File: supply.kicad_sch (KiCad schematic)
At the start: 98 parts, among them J12 Molex_Nano-Fit-105430_xx02-ho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, Q11 PJE138K, Q13 BCM857BS-7-F, Q14 BCM857BS-7-F, Q15 SSM3J332R, Q16 SSM3J332R, Q18 SSM3J332R, Q5 PJE138K, Q6 SSM3J332R, Q7 PJE138K, Q8 PJE138K, SW1 PCM12SMTR, U1 TPS56C230, U29 TPS56C230, U37 74LVC2G14GV, U38 74LVC1G175GV, U41 NCP730BMT330TBG, U42 TPS7A0518PDBVT

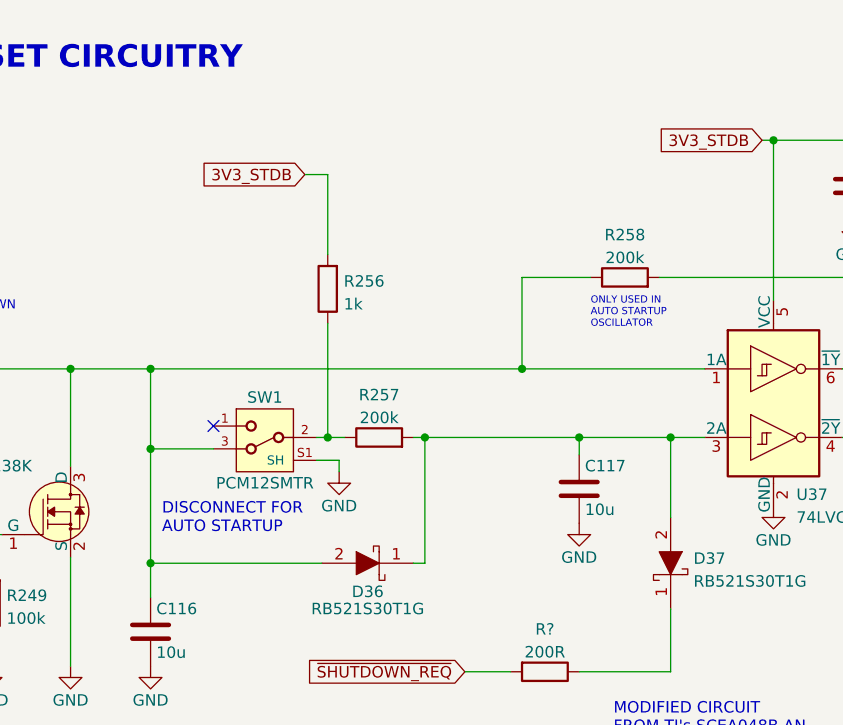
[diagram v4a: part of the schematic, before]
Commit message: Clarify auto startup comments
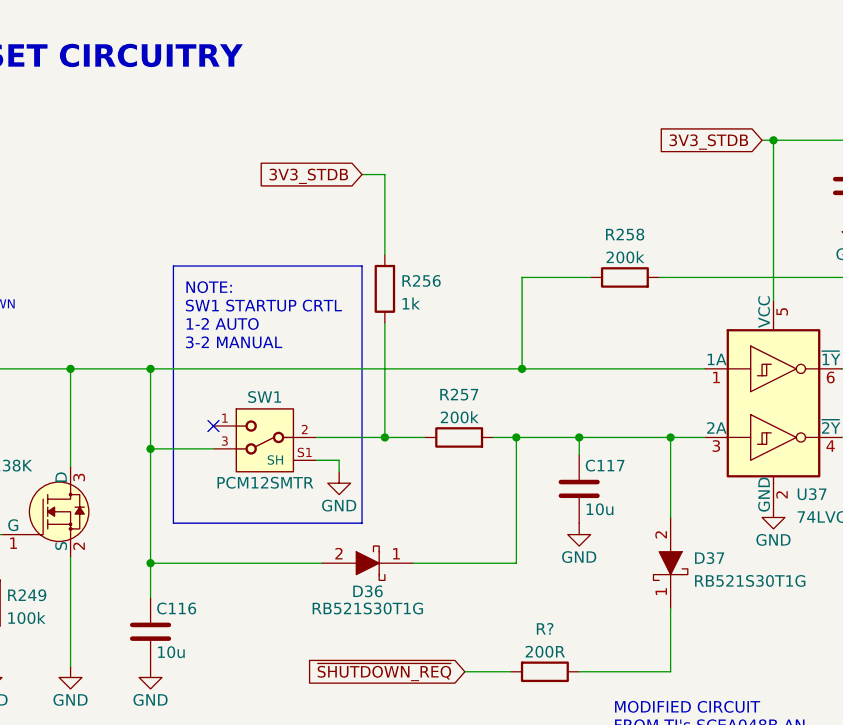
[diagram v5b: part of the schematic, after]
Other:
- note added: "NOTE: SW1 STARTUP CRTL 1-2 AUTO 3-2 MANUAL"
- note removed: "DISCONNECT FOR AUTO STARTUP"
- note removed: "ONLY USED IN AUTO STARTUP OSCILLATOR"
- moved on the sheet: R256, R257
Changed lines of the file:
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@@
   (junction (at 148.59 52.07) (diameter 0) (color 0 0 0 0)
   )
-  (junction (at 88.9 59.69) (diameter 0) (color 0 0 0 0)
-  )
   (junction (at 365.76 71.12) (diameter 0) (color 0 0 0 0)
   )
@@
   (junction (at 58.42 146.05) (diameter 0) (color 0 0 0 0)
   )
+  (junction (at 95.25 59.69) (diameter 0) (color 0 0 0 0)
+  )
   (junction (at 231.14 57.15) (diameter 0) (color 0 0 0 0)
   )
@@
   (junction (at 347.98 125.73) (diameter 0) (color 0 0 0 0)
   )
-  (junction (at 99.695 59.69) (diameter 0) (color 0 0 0 0)
-  )
   (junction (at 190.5 41.91) (diameter 0) (color 0 0 0 0)
   )
   (junction (at 134.62 129.54) (diameter 0) (color 0 0 0 0)
   )
+  (junction (at 109.855 59.69) (diameter 0) (color 0 0 0 0)
+  )
   (junction (at 224.79 120.65) (diameter 0) (color 0 0 0 0)
   )
@@
     (stroke (width 0) (type default) (color 0 0 0 0))
   )
+  (polyline (pts (xy 92.71 69.215) (xy 92.71 40.64))
+    (stroke (width 0) (type default) (color 0 0 0 0))
+  )
   (wire (pts (xy 240.03 40.64) (xy 242.57 40.64))
     (stroke (width 0) (type default) (color 0 0 0 0))
@@
     (stroke (width 0) (type default) (color 0 0 0 0))
   )
+  (wire (pts (xy 109.855 59.69) (xy 116.84 59.69))
+    (stroke (width 0) (type default) (color 0 0 0 0))
+  )
   (wire (pts (xy 245.11 210.82) (xy 245.11 219.71))
     (stroke (width 0) (type default) (color 0 0 0 0))
@@
     (stroke (width 0) (type default) (color 0 0 0 0))
   )
-  (wire (pts (xy 88.9 46.99) (xy 88.9 59.69))
+  (wire (pts (xy 95.25 46.99) (xy 95.25 59.69))
     (stroke (width 0) (type default) (color 0 0 0 0))
   )
@@
     (stroke (width 0) (type default) (color 0 0 0 0))
   )
-  (wire (pts (xy 88.9 30.48) (xy 88.9 39.37))
+  (wire (pts (xy 95.25 30.48) (xy 95.25 39.37))
     (stroke (width 0) (type default) (color 0 0 0 0))
   )
@@
     (stroke (width 0) (type default) (color 0 0 0 0))
   )
+  (wire (pts (xy 95.25 59.69) (xy 99.695 59.69))
+    (stroke (width 0) (type default) (color 0 0 0 0))
+  )
   (wire (pts (xy 382.27 29.21) (xy 382.27 30.48))
     (stroke (width 0) (type default) (color 0 0 0 0))
@@
     (stroke (width 0) (type default) (color 0 0 0 0))
   )
+  (polyline (pts (xy 71.755 69.215) (xy 92.71 69.215))
+    (stroke (width 0) (type default) (color 0 0 0 0))
+  )
   (wire (pts (xy 375.92 125.73) (xy 382.27 125.73))
     (stroke (width 0) (type default) (color 0 0 0 0))
@@
     (stroke (width 0) (type default) (color 0 0 0 0))
   )
+  (polyline (pts (xy 71.755 40.64) (xy 71.755 69.215))
+    (stroke (width 0) (type default) (color 0 0 0 0))
+  )
   (wire (pts (xy 242.57 44.45) (xy 242.57 45.085))
     (stroke (width 0) (type default) (color 0 0 0 0))
@@
     (stroke (width 0) (type default) (color 0 0 0 0))
   )
-  (wire (pts (xy 98.425 73.66) (xy 99.695 73.66))
+  (wire (pts (xy 98.425 73.66) (xy 109.855 73.66))
     (stroke (width 0) (type default) (color 0 0 0 0))
   )
@@
     (stroke (width 0) (type default) (color 0 0 0 0))
   )
-  (wire (pts (xy 87.63 59.69) (xy 88.9 59.69))
-    (stroke (width 0) (type default) (color 0 0 0 0))
-  )
   (wire (pts (xy 60.325 73.025) (xy 60.325 85.09))
     (stroke (width 0) (type default) (color 0 0 0 0))
@@
     (stroke (width 0) (type default) (color 0 0 0 0))
   )
-  (wire (pts (xy 98.425 59.69) (xy 99.695 59.69))
+  (polyline (pts (xy 71.755 40.64) (xy 92.71 40.64))
     (stroke (width 0) (type default) (color 0 0 0 0))
   )
@@
     (stroke (width 0) (type default) (color 0 0 0 0))
   )
-  (wire (pts (xy 88.9 59.69) (xy 90.805 59.69))
+  (wire (pts (xy 87.63 59.69) (xy 95.25 59.69))
     (stroke (width 0) (type default) (color 0 0 0 0))
   )
@@
     (stroke (width 0) (type default) (color 0 0 0 0))
   )
-  (wire (pts (xy 280.67 200.66) (xy 292.1 200.66))
+  (wire (pts (xy 107.315 59.69) (xy 109.855 59.69))
     (stroke (width 0) (type default) (color 0 0 0 0))
   )
-  (wire (pts (xy 360.68 81.28) (xy 360.68 82.55))
+  (wire (pts (xy 280.67 200.66) (xy 292.1 200.66))
     (stroke (width 0) (type default) (color 0 0 0 0))
   )
-  (wire (pts (xy 99.695 59.69) (xy 116.84 59.69))
+  (wire (pts (xy 360.68 81.28) (xy 360.68 82.55))
     (stroke (width 0) (type default) (color 0 0 0 0))
   )
@@
     (stroke (width 0) (type default) (color 0 0 0 0))
   )
-  (wire (pts (xy 88.9 30.48) (xy 86.36 30.48))
+  (wire (pts (xy 95.25 30.48) (xy 92.71 30.48))
     (stroke (width 0) (type default) (color 0 0 0 0))
   )
@@
     (stroke (width 0) (type default) (color 0 0 0 0))
   )
-  (wire (pts (xy 99.695 73.66) (xy 99.695 59.69))
+  (wire (pts (xy 109.855 73.66) (xy 109.855 59.69))
     (stroke (width 0) (type default) (color 0 0 0 0))
   )
@@
     (effects (font (size 1.27 1.27)) (justify left bottom))
   )
-  (text "ONLY USED IN\nAUTO STARTUP\nOSCILLATOR" (at 118.11 47.625 0)
-    (effects (font (size 0.8 0.8)) (justify left bottom))
-  )
   (text "3V3 STANDBY LDO" (at 290.83 17.78 0)
     (effects (font (size 2.5 2.5) bold) (justify left bottom))
@@
     (effects (font (size 2.5 2.5) bold) (justify left bottom))
   )
-  (text "DISCONNECT FOR\nAUTO STARTUP\n" (at 70.485 70.485 0)
+  (text "NOTE:\nSW1 STARTUP CRTL\n1-2 AUTO \n3-2 MANUAL" (at 73.025 50.165 0)
     (effects (font (size 1.27 1.27)) (justify left bottom))
   )
@@
     )
   )
-  (global_label "3V3_STDB" (shape input) (at 86.36 30.48 180) (fields_autoplaced)
+  (global_label "3V3_STDB" (shape input) (at 92.71 30.48 180) (fields_autoplaced)
     (effects (font (size 1.27 1.27)) (justify right))
-    (property "Intersheet References" "${INTERSHEET_REFS}" (id 0) (at 74.7545 30.5594 0)
+    (property "Intersheet References" "${INTERSHEET_REFS}" (id 0) (at 81.1045 30.5594 0)
       (effects (font (size 1.27 1.27)) (justify right))
     )
@@
     (pin "3")
   )
-  (symbol (lib_id "jetson-orin-baseboard:R_200k_0402") (at 94.615 59.69 0) (unit 1)
+  (symbol (lib_id "jetson-orin-baseboard:R_200k_0402") (at 103.505 59.69 0) (unit 1)
     (in_bom yes) (on_board yes) (fields_autoplaced)
-    (property "Reference" "R257" (id 0) (at 94.615 54.9742 0))
-    (property "Value" "R_200k_0402" (id 1) (at 94.615 63.5 0)
+    (property "Reference" "R257" (id 0) (at 103.505 54.9742 0))
+    (property "Value" "R_200k_0402" (id 1) (at 103.505 63.5 0)
       (effects (font (size 1.27 1.27)) hide)
     )
-    (property "Footprint" "jetson-orin-baseboard-footprints:0402-res" (id 2) (at 99.695 54.61 0)
+    (property "Footprint" "jetson-orin-baseboard-footprints:0402-res" (id 2) (at 108.585 54.61 0)
       (effects (font (size 1.524 1.524)) (justify left) hide)
     )
-    (property "Datasheet" "" (id 3) (at 94.615 59.69 0)
+    (property "Datasheet" "" (id 3) (at 103.505 59.69 0)
       (effects (font (size 1.27 1.27)) hide)
     )
-    (property "Manufacturer" "YAGEO_(PHYCOMP)" (id 4) (at 99.695 49.53 0)
+    (property "Manufacturer" "YAGEO_(PHYCOMP)" (id 4) (at 108.585 49.53 0)
       (effects (font (size 1.524 1.524)) (justify left) hide)
     )
-    (property "MPN" "RC0402FR-07200KL" (id 5) (at 99.695 52.07 0)
+    (property "MPN" "RC0402FR-07200KL" (id 5) (at 108.585 52.07 0)
       (effects (font (size 1.524 1.524)) (justify left) hide)
     )
-    (property "Val" "200k" (id 6) (at 94.615 57.5111 0))
+    (property "Val" "200k" (id 6) (at 103.505 57.5111 0))
     (pin "1")
     (pin "2")
@@
     (pin "2")
   )
-  (symbol (lib_id "jetson-orin-baseboard:R_1k_0402") (at 88.9 43.18 90) (unit 1)
+  (symbol (lib_id "jetson-orin-baseboard:R_1k_0402") (at 95.25 43.18 90) (unit 1)
     (in_bom yes) (on_board yes) (fields_autoplaced)
-    (property "Reference" "R256" (id 0) (at 90.678 42.3453 90)
+    (property "Reference" "R256" (id 0) (at 97.028 42.3453 90)
       (effects (font (size 1.27 1.27)) (justify right))
     )
-    (property "Value" "R_1k_0402" (id 1) (at 92.71 43.18 0)
+    (property "Value" "R_1k_0402" (id 1) (at 99.06 43.18 0)
       (effects (font (size 1.27 1.27)) hide)
     )
-    (property "Footprint" "jetson-orin-baseboard-footprints:0402-res" (id 2) (at 83.82 38.1 0)
+    (property "Footprint" "jetson-orin-baseboard-footprints:0402-res" (id 2) (at 90.17 38.1 0)
       (effects (font (size 1.524 1.524)) (justify left) hide)
     )
-    (property "Datasheet" "" (id 3) (at 88.9 43.18 0)
+    (property "Datasheet" "" (id 3) (at 95.25 43.18 0)
       (effects (font (size 1.27 1.27)) hide)
     )
-    (property "Manufacturer" "BOURNS" (id 4) (at 78.74 38.1 0)
+    (property "Manufacturer" "BOURNS" (id 4) (at 85.09 38.1 0)
       (effects (font (size 1.524 1.524)) (justify left) hide)
     )
-    (property "MPN" "CR0402-FX-1001GLF" (id 5) (at 81.28 38.1 0)
+    (property "MPN" "CR0402-FX-1001GLF" (id 5) (at 87.63 38.1 0)
       (effects (font (size 1.524 1.524)) (justify left) hide)
     )
-    (property "Val" "1k" (id 6) (at 90.678 44.8822 90)
+    (property "Val" "1k" (id 6) (at 97.028 44.8822 90)
       (effects (font (size 1.27 1.27)) (justify right))
     )

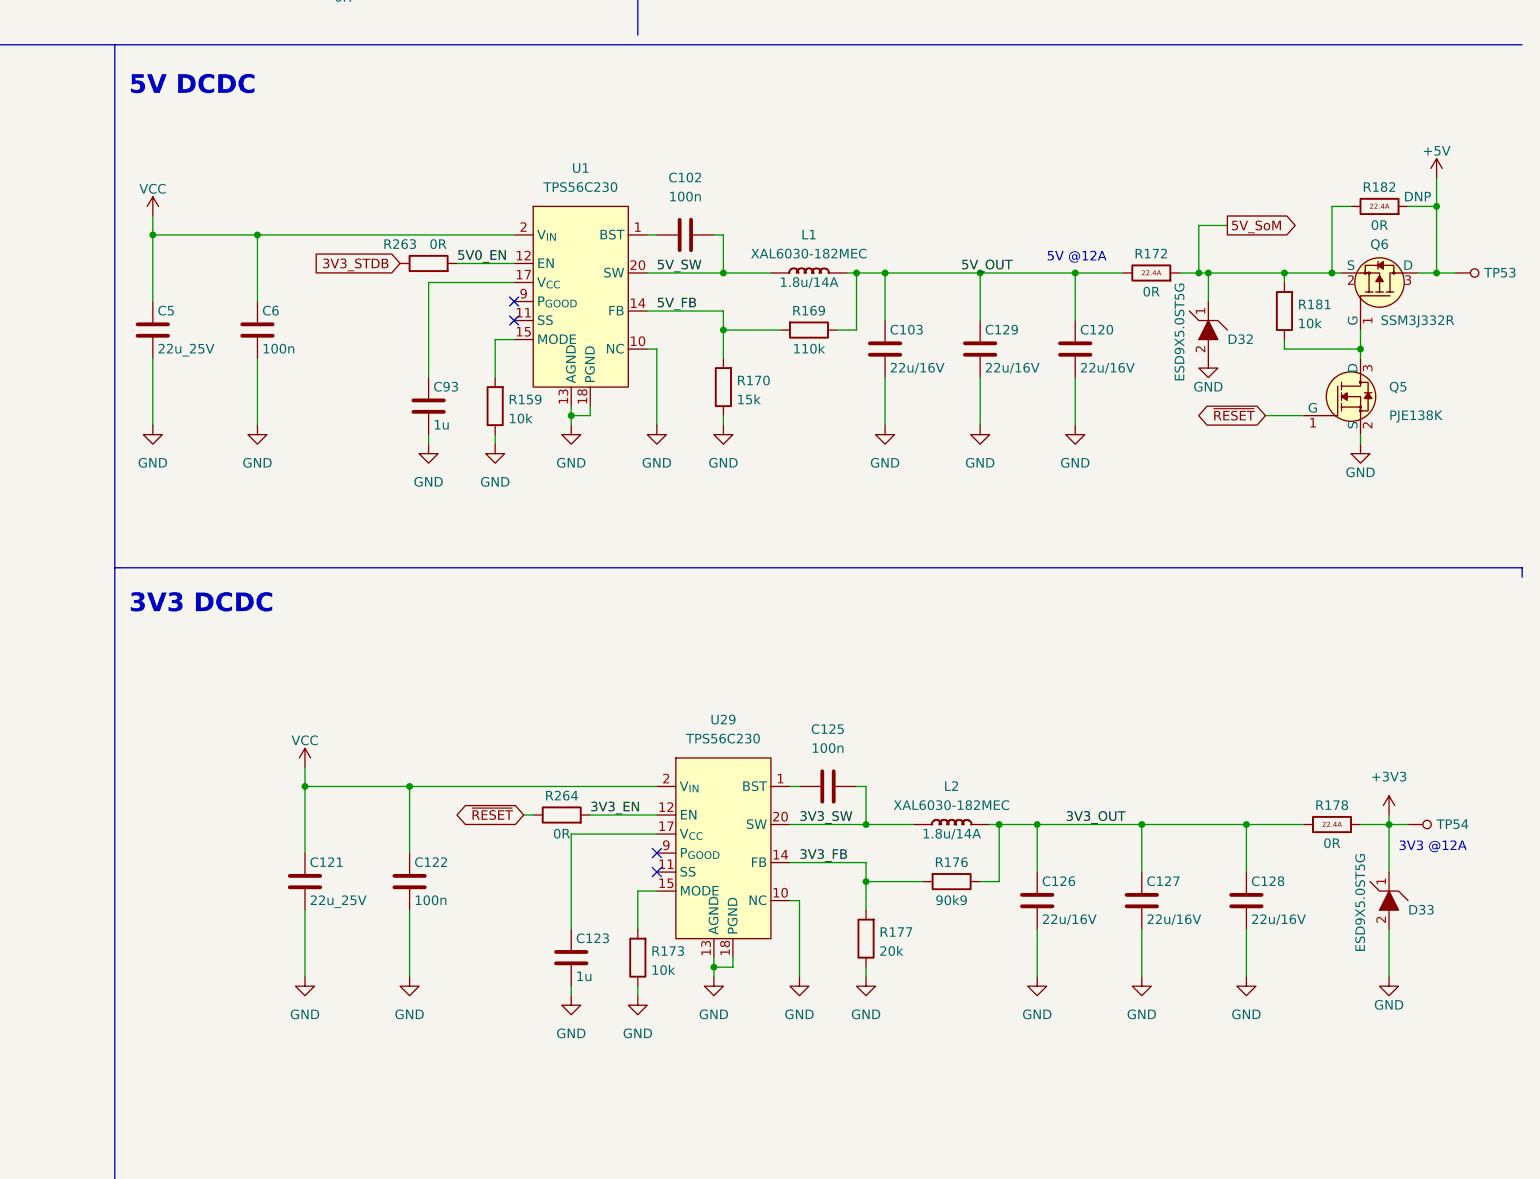
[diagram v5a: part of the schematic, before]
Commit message: Update TPS56C230 symbol. Add more capacitors to the 5V and 3.3V DCDCs
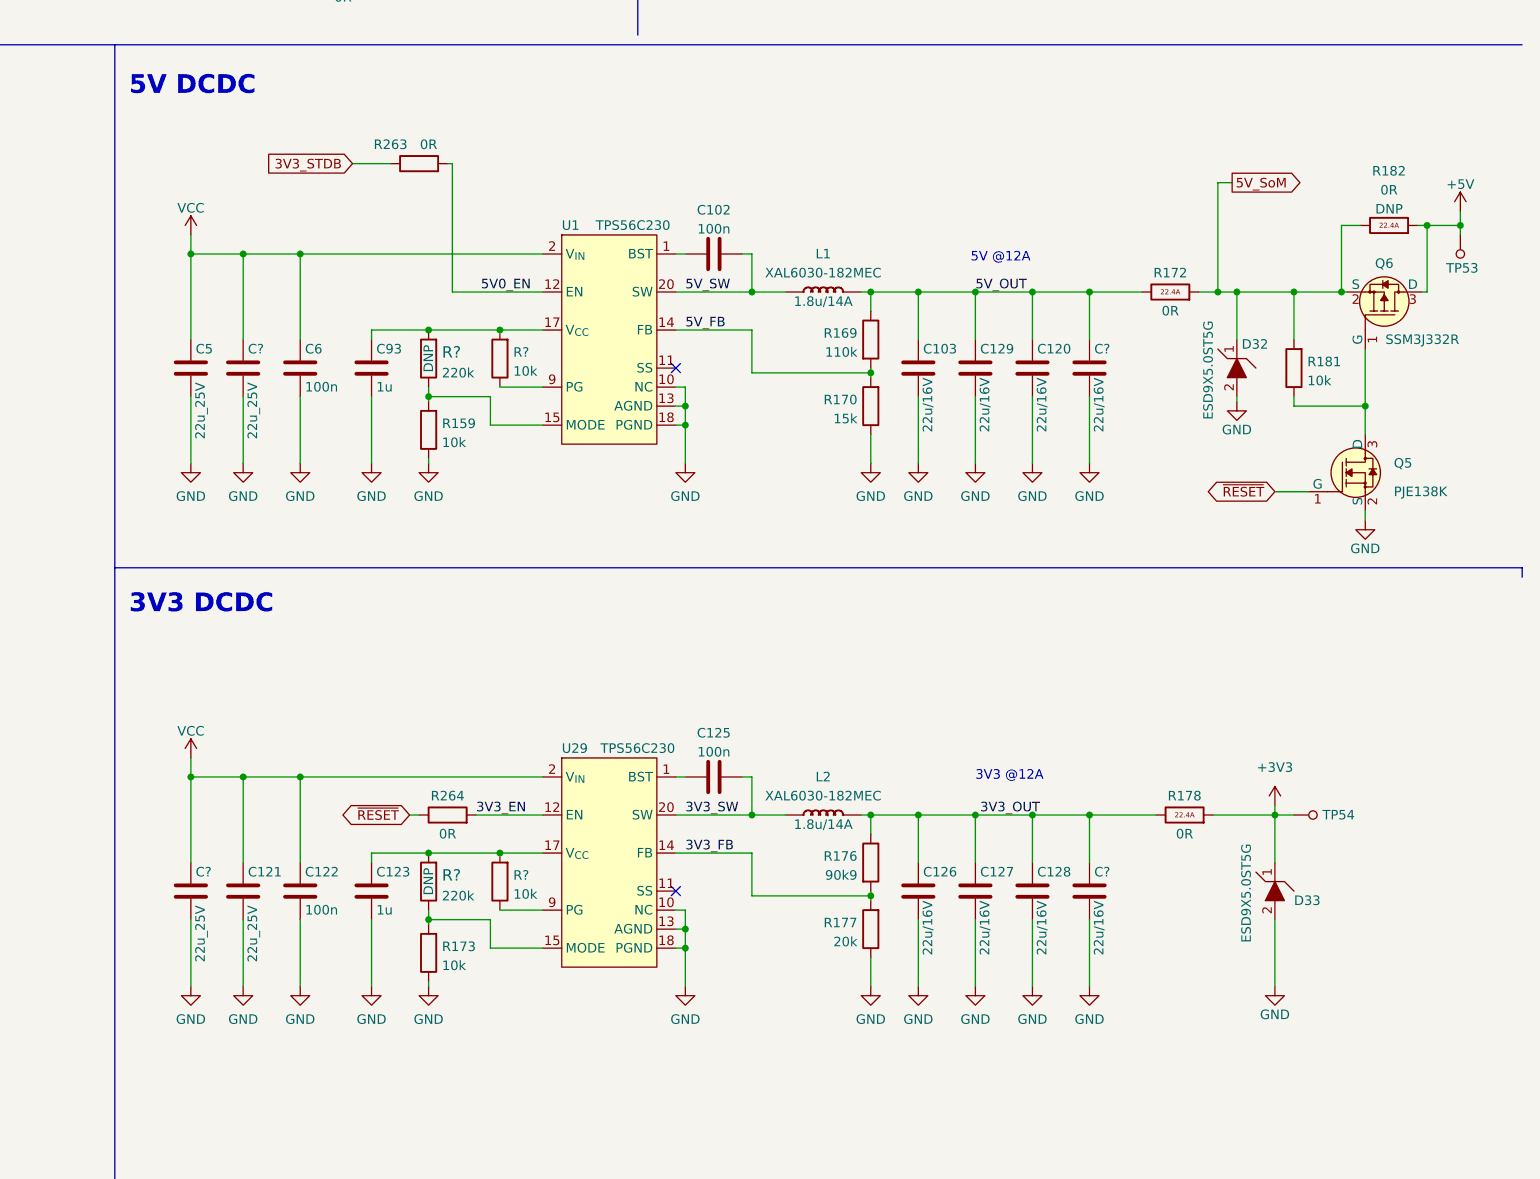
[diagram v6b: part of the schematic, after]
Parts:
- added C? (x2): C_22u_0603_16V, antmicro-footprints:0603-cap, symbol antmicroCapacitors0603:C_22u_0603_16V
- added C? (x2): C_22u_0805_25V, antmicro-footprints:0805-cap, symbol antmicroCapacitorsmisc:C_22u_0805_25V
- added R? (x2): R_220k_0402, antmicro-footprints:0402-res, symbol antmicroResistors0402:R_220k_0402
- added R? (x2): R_10k_0402, jetson-orin-baseboard-footprints:0402-res, symbol jetson-orin-baseboard:R_10k_0402
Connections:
- net 3V3_OUT: now also C?.1
- net 5V_OUT: now also C?.1
- net GND: now also C?.2, C?.2, C?.2, C?.2
- net VCC: now also C?.1, C?.1
- net at R159.2, U1.15 (MODE): now also R?.1
- net at C93.1, U1.17 (V_{CC}): now also R?.2, R?.2
- net at U1.9 (PG): now also R?.1
- net at R173.2, U29.15 (MODE): now also R?.1
- net at C123.1, U29.17 (V_{CC}): now also R?.2, R?.2
- net at U29.9 (PG): now also R?.1
- no-connect marks 5 -> 3
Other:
- moved on the sheet: C102, C103, C120, C121, C122, C123, C125, C126, C127, C128, C129, C5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
